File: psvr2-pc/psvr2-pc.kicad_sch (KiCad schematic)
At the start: 12 parts, among them J2 USB3_B_Micro, J3 DP_47272, J4 USB_C_Receptacle_USB2.0_14P, P1 USB_C_Plug, Q1 IRLML6244, U1 RP2040, U2 M95256-WMN6P, U3 FUSB302B01MPX, U4 FUSB302B01MPX, Y1 Crystal

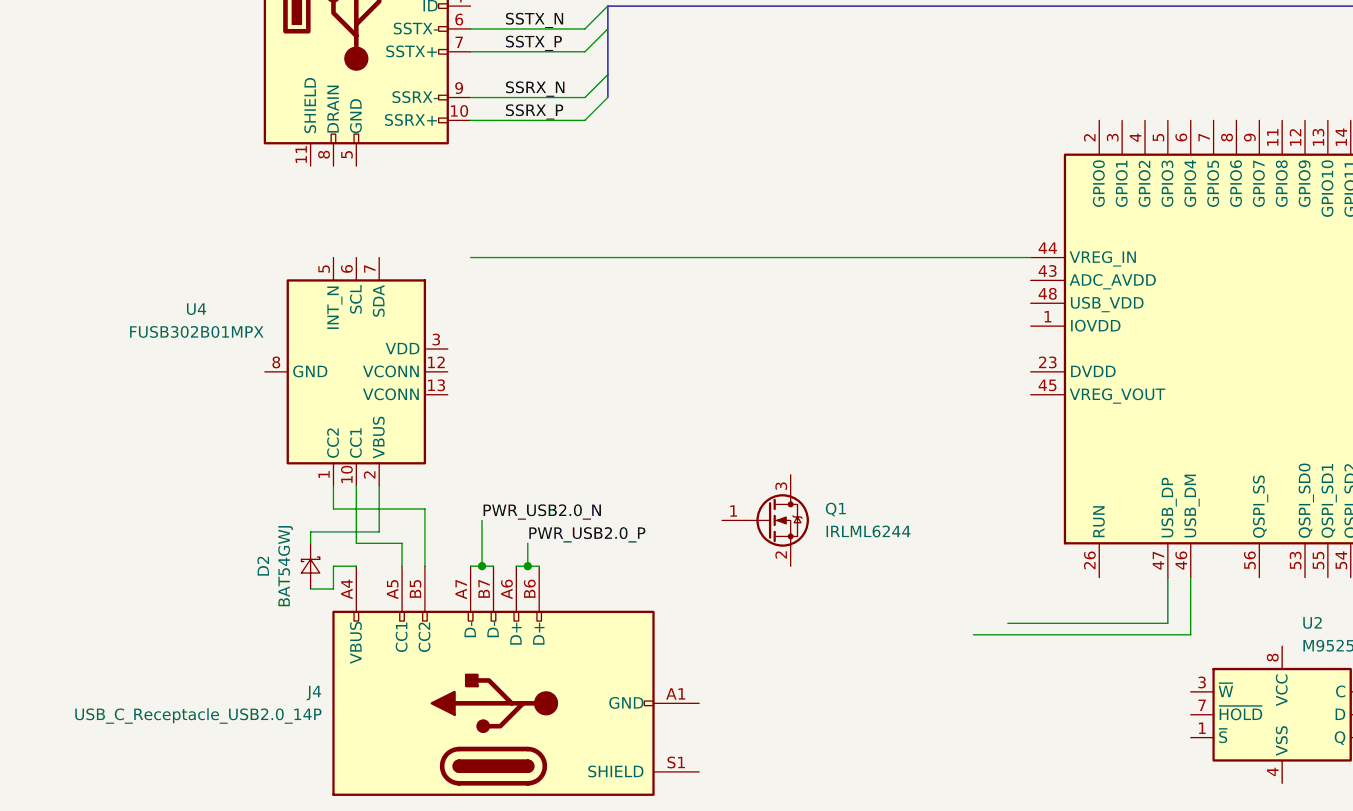
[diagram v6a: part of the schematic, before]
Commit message: Clean up the wiring. Move some stuff around.
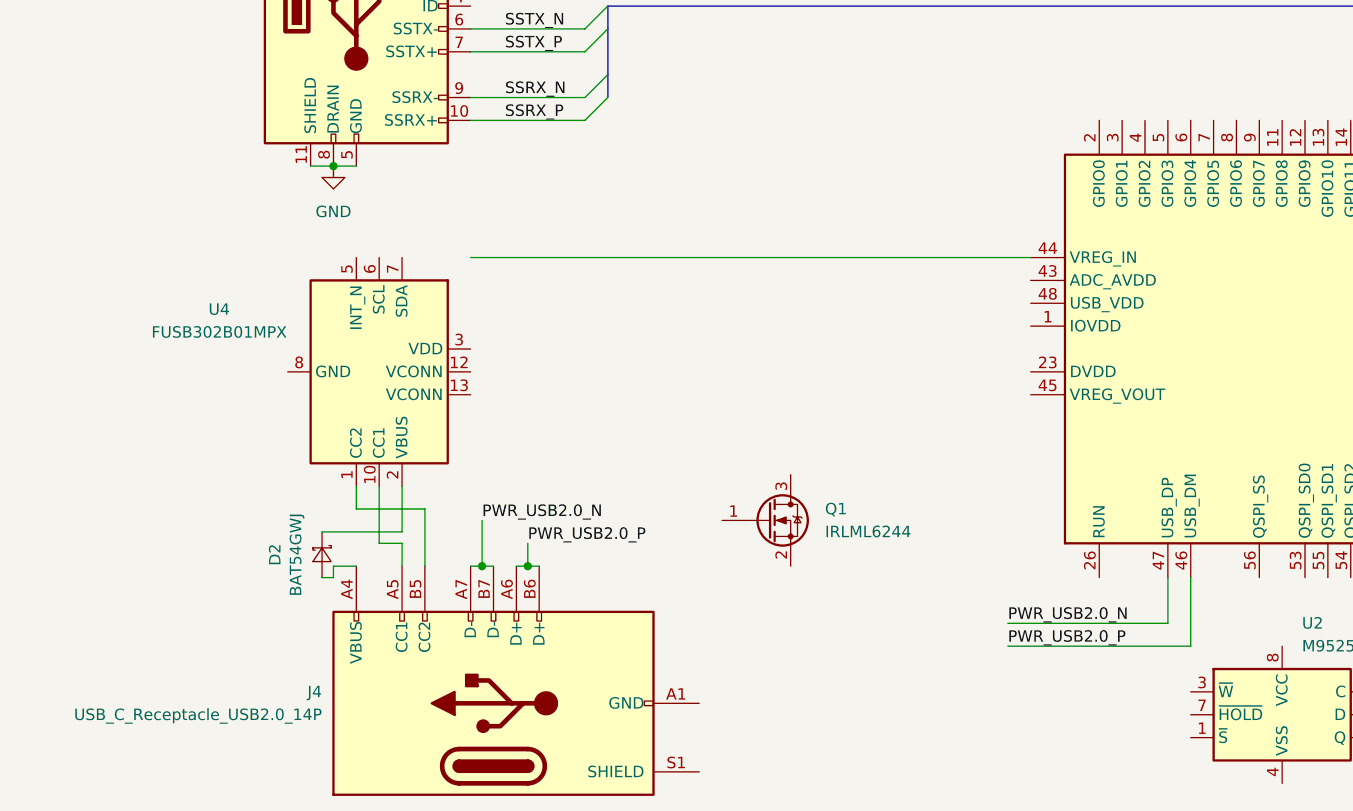
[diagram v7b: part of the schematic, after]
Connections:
- net GND: now also J2.11 (SHIELD), J2.5 (GND), J2.8 (DRAIN)
- net PWR_USB2.0_N: now also U1.47 (USB_DP)
- net PWR_USB2.0_P: now also U1.46 (USB_DM)
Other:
- moved on the sheet: D2, U4
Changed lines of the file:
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@@
   (junction (at 43.18 69.85) (diameter 0) (color 0 0 0 0)
   )
+  (junction (at 25.4 113.03) (diameter 0) (color 0 0 0 0)
+  )
   (junction (at 41.91 157.48) (diameter 0) (color 0 0 0 0)
   )
@@
     (stroke (width 0) (type default))
   )
+  (wire (pts (xy 25.4 113.03) (xy 27.94 113.03))
+    (stroke (width 0) (type default))
+  )
   (wire (pts (xy 240.03 90.17) (xy 252.73 90.17))
     (stroke (width 0) (type default))
@@
     (stroke (width 0) (type default))
   )
-  (wire (pts (xy 27.94 148.59) (xy 27.94 154.94))
+  (wire (pts (xy 30.48 148.59) (xy 30.48 154.94))
     (stroke (width 0) (type default))
   )
@@
     (stroke (width 0) (type default))
   )
-  (wire (pts (xy 120.65 165.1) (xy 120.65 158.75))
+  (wire (pts (xy 120.65 158.75) (xy 120.65 166.37))
     (stroke (width 0) (type default))
   )
@@
     (stroke (width 0) (type default))
   )
+  (wire (pts (xy 120.65 166.37) (xy 100.33 166.37))
+    (stroke (width 0) (type default))
+  )
   (wire (pts (xy 41.91 157.48) (xy 43.18 157.48))
     (stroke (width 0) (type default))
@@
     (stroke (width 0) (type default))
   )
-  (wire (pts (xy 96.52 165.1) (xy 120.65 165.1))
-    (stroke (width 0) (type default))
-  )
   (bus (pts (xy 55.88 20.32) (xy 55.88 27.94))
     (stroke (width 0) (type default))
@@
     (stroke (width 0) (type default))
   )
-  (wire (pts (xy 22.86 153.67) (xy 30.48 153.67))
+  (wire (pts (xy 24.13 153.67) (xy 33.02 153.67))
     (stroke (width 0) (type default))
   )
@@
     (stroke (width 0) (type default))
   )
-  (wire (pts (xy 25.4 148.59) (xy 25.4 151.13))
+  (wire (pts (xy 27.94 148.59) (xy 27.94 151.13))
     (stroke (width 0) (type default))
   )
@@
     (stroke (width 0) (type default))
   )
-  (wire (pts (xy 25.4 151.13) (xy 35.56 151.13))
+  (wire (pts (xy 27.94 151.13) (xy 35.56 151.13))
     (stroke (width 0) (type default))
   )
@@
     (stroke (width 0) (type default))
   )
-  (wire (pts (xy 27.94 154.94) (xy 33.02 154.94))
+  (wire (pts (xy 30.48 154.94) (xy 33.02 154.94))
     (stroke (width 0) (type default))
   )
@@
     (stroke (width 0) (type default))
   )
+  (wire (pts (xy 22.86 113.03) (xy 25.4 113.03))
+    (stroke (width 0) (type default))
+  )
   (wire (pts (xy 43.18 33.02) (xy 43.18 40.64))
     (stroke (width 0) (type default))
@@
     (stroke (width 0) (type default))
   )
-  (wire (pts (xy 25.4 160.02) (xy 25.4 157.48))
+  (wire (pts (xy 25.4 158.75) (xy 25.4 157.48))
     (stroke (width 0) (type default))
   )
@@
     (stroke (width 0) (type default))
   )
-  (wire (pts (xy 22.86 160.02) (xy 25.4 160.02))
+  (wire (pts (xy 24.13 158.75) (xy 25.4 158.75))
     (stroke (width 0) (type default))
   )
@@
     (stroke (width 0) (type default))
   )
-  (wire (pts (xy 22.86 153.67) (xy 22.86 154.94))
-    (stroke (width 0) (type default))
-  )
   (wire (pts (xy 240.03 74.93) (xy 252.73 74.93))
     (stroke (width 0) (type default))
   )
-  (wire (pts (xy 30.48 148.59) (xy 30.48 153.67))
+  (wire (pts (xy 33.02 148.59) (xy 33.02 153.67))
     (stroke (width 0) (type default))
   )
@@
     (effects (font (size 1.27 1.27)) (justify left bottom))
   )
+  (label "PWR_USB2.0_P" (at 100.33 166.37 0) (fields_autoplaced)
+    (effects (font (size 1.27 1.27)) (justify left bottom))
+  )
   (label "ML1_N" (at 242.57 87.63 0) (fields_autoplaced)
     (effects (font (size 1.27 1.27)) (justify left bottom))
   )
   (label "SSRX_P" (at 44.45 107.95 0) (fields_autoplaced)
+    (effects (font (size 1.27 1.27)) (justify left bottom))
+  )
+  (label "PWR_USB2.0_N" (at 100.33 163.83 0) (fields_autoplaced)
     (effects (font (size 1.27 1.27)) (justify left bottom))
   )
@@
     )
   )
-  (symbol (lib_id "Interface_USB:FUSB302B01MPX") (at 27.94 135.89 270) (unit 1)
-    (in_bom yes) (on_board yes) (dnp no) (fields_autoplaced)
-    (property "Reference" "U4" (at 10.16 128.9619 90)
-      (effects (font (size 1.27 1.27)))
-    )
-    (property "Value" "FUSB302B01MPX" (at 10.16 131.5019 90)
-      (effects (font (size 1.27 1.27)))
-    )
-    (property "Footprint" "Package_DFN_QFN:WQFN-14-1EP_2.5x2.5mm_P0.5mm_EP1.45x1.45mm" (at 15.24 135.89 0)
-      (effects (font (size 1.27 1.27)) hide)
-    )
-    (property "Datasheet" "http://www.onsemi.com/pub/Collateral/FUSB302B-D.PDF" (at 17.78 138.43 0)
+  (symbol (lib_id "Interface_USB:FUSB302B01MPX") (at 30.48 135.89 270) (unit 1)
+    (in_bom yes) (on_board yes) (dnp no) (fields_autoplaced)
+    (property "Reference" "U4" (at 12.7 128.9619 90)
+      (effects (font (size 1.27 1.27)))
+    )
+    (property "Value" "FUSB302B01MPX" (at 12.7 131.5019 90)
+      (effects (font (size 1.27 1.27)))
+    )
+    (property "Footprint" "Package_DFN_QFN:WQFN-14-1EP_2.5x2.5mm_P0.5mm_EP1.45x1.45mm" (at 17.78 135.89 0)
+      (effects (font (size 1.27 1.27)) hide)
+    )
+    (property "Datasheet" "http://www.onsemi.com/pub/Collateral/FUSB302B-D.PDF" (at 20.32 138.43 0)
       (effects (font (size 1.27 1.27)) hide)
     )
@@
     )
   )
-  (symbol (lib_id "DPSwitch-rescue:BAT54GWJ-visclib") (at 22.86 157.48 270) (unit 1)
+  (symbol (lib_id "DPSwitch-rescue:BAT54GWJ-visclib") (at 24.13 156.21 270) (unit 1)
     (in_bom yes) (on_board yes) (dnp no)
-    (property "Reference" "D2" (at 17.653 157.48 0)
-      (effects (font (size 1.27 1.27)))
-    )
-    (property "Value" "BAT54GWJ" (at 19.9644 157.48 0)
-      (effects (font (size 1.27 1.27)))
-    )
-    (property "Footprint" "Diodes_SMD:D_SOD-123" (at 22.86 157.48 90)
-      (effects (font (size 1.27 1.27)) hide)
-    )
-    (property "Datasheet" "~" (at 22.86 157.48 90)
+    (property "Reference" "D2" (at 18.923 156.21 0)
+      (effects (font (size 1.27 1.27)))
+    )
+    (property "Value" "BAT54GWJ" (at 21.2344 156.21 0)
+      (effects (font (size 1.27 1.27)))
+    )
+    (property "Footprint" "Diodes_SMD:D_SOD-123" (at 24.13 156.21 90)
+      (effects (font (size 1.27 1.27)) hide)
+    )
+    (property "Datasheet" "~" (at 24.13 156.21 90)
       (effects (font (size 1.27 1.27)) hide)
     )
@@
         )
       )
+    )
+  )
+  (symbol (lib_id "power:GND") (at 25.4 113.03 0) (unit 1)
+    (in_bom yes) (on_board yes) (dnp no) (fields_autoplaced)
+    (property "Reference" "#PWR04" (at 25.4 119.38 0)
+      (effects (font (size 1.27 1.27)) hide)
+    )
+    (property "Value" "GND" (at 25.4 118.11 0)
+      (effects (font (size 1.27 1.27)))
+    )
+    (property "Footprint" "" (at 25.4 113.03 0)
+      (effects (font (size 1.27 1.27)) hide)
+    )
+    (property "Datasheet" "" (at 25.4 113.03 0)
+      (effects (font (size 1.27 1.27)) hide)
+    )
+    (pin "1")
+    (instances
+      (project "psvr2-pc"
+        (path "/381748c8-fb8a-4e0a-a26e-44fd86369b77"
+          (reference "#PWR04") (unit 1)
+        )
+      )

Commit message: Mess around with KiBuzzard and the PCB Editor.
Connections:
- net USB2.0_P: now also J2.3 (D+)
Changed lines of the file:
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@@
+    (stroke (width 0) (type default))
+  )
+  (wire (pts (xy 40.64 92.71) (xy 44.45 92.71))
     (stroke (width 0) (type default))
   )
